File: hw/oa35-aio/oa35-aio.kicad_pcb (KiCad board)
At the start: 6 copper layers, 36 x 36 mm, 283 parts, among them J1 TYPE-C-31-M-12, J10 M1A, J11 M1B, J12 M1C, J13 M2A, J14 M2B, J15 M2C, J16 M3A, J17 M3B, J18 M3C, J19 M4A, J2 SM06B-SRSS-TB, J20 M4B, J21 M4C, J3 BAT+, J4 BAT-, P1 +5V, P10 TX6, P11 RX1, P12 TX1, P13 LED, P14 BZ-, P15 BZ+, P16 RSSI, P17 SCL, P18 SDA, P19 +3V3, P2 GND, P20 GND, P21 VBAT, P22 GND, P3 RX2, P4 TX2, P5 +5V, P6 GND, P7 RX4, P8 TX4, P9 RX6, Q1 2N7002, U1 INA186A3IDCKR, U10 USBLC6-2SC6, U2 LMR51430YFDDCR, U20 AT32F421G8U7, U21 NSG2065Q, U3 LMR51430YFDDCR, U30 AT32F421G8U7, U31 NSG2065Q, U4 LP5912-3.3DRVR, U40 AT32F421G8U7, U41 NSG2065Q, U5 TLV76733DRVR, U50 AT32F421G8U7, U51 NSG2065Q, U6 STM32F722RET6, U7 ICM-42688-P, U8 BMP280, U9 W25Q128JVSIQ, Y1 8MHz

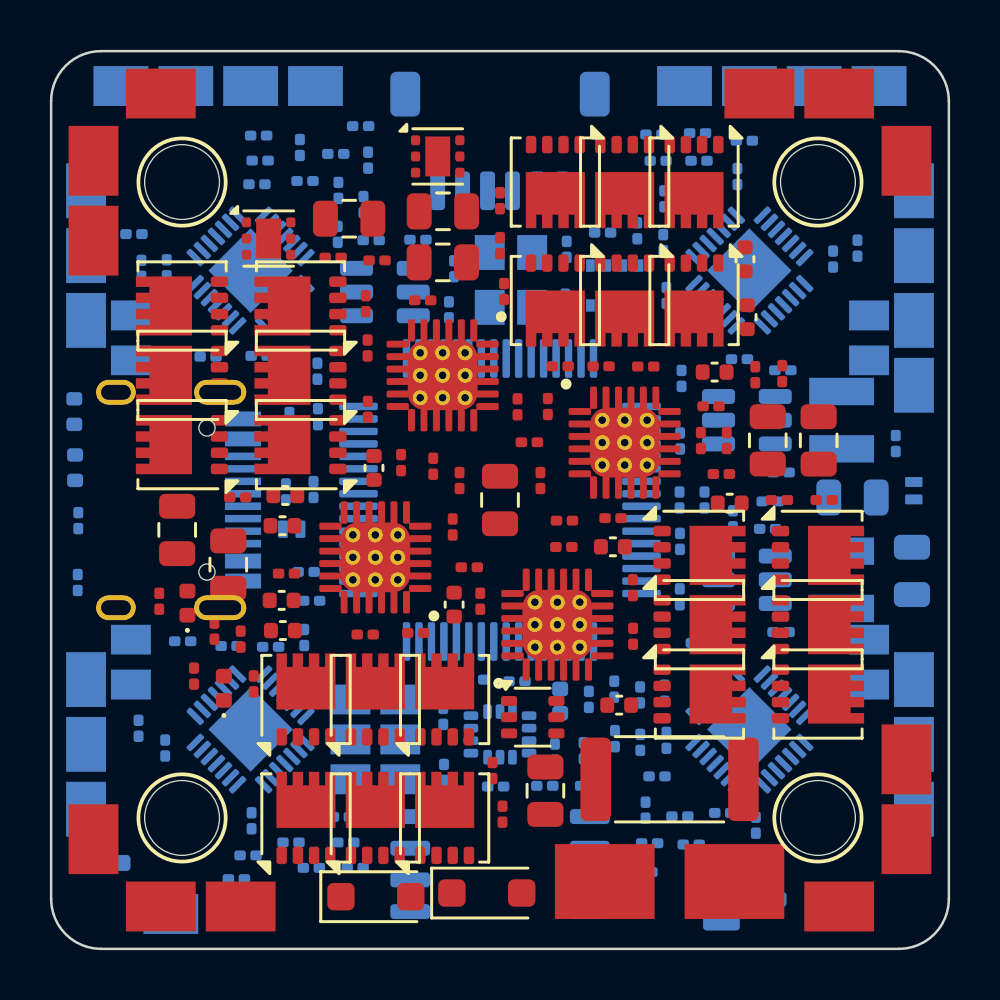
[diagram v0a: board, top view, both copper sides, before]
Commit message: OA35-AIO: fix current-sense input polarity and LDO no-connects
The INA186 in DCK/SC70-6 is 1 REF, 2 GND, 3 VS, 4 IN+, 5 IN-, 6 OUT, per
KiCad's own INA199xxDCK symbol and the OpenESC symbol library. High-side
sensing needs IN+ on the battery side of the shunt; the reference design
wires it the other way round, which would read zero current. Corrected here
and documented.

Also stop tying the LP5912's NC and open-drain power-good pins to rails, and
give the auto-placer "sit next to X" hints so decoupling lands on the pin it
decouples (mean distance 4.6 mm instead of 6.9 mm).

Co-Authored-By: Claude Opus 5 <noreply@anthropic.com>
Claude-Session: https://claude.ai/code/session_013J1rgXZWykCJN7jVVS67P2
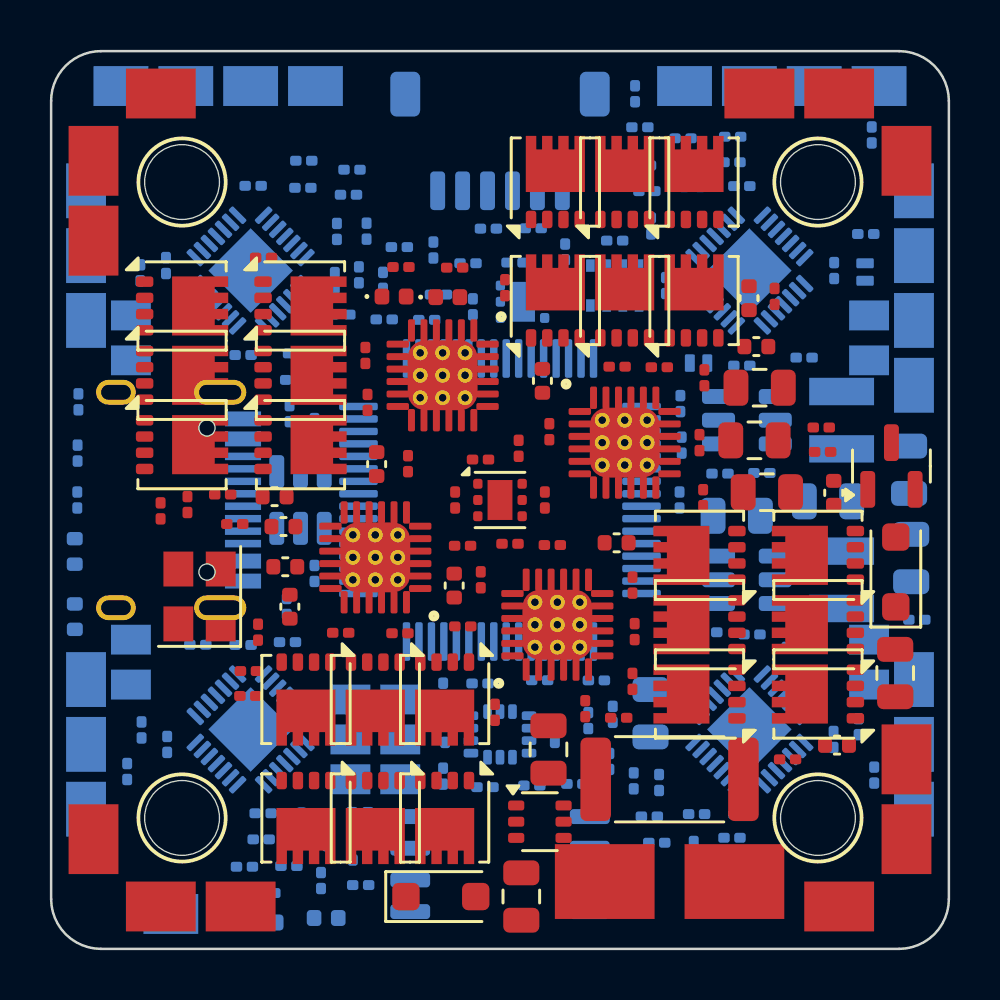
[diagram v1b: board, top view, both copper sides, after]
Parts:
- C10, C11, C16, C17, C18, C24, C25, C26, C29, C30, C38, C40, C41, C9, U5: moved to B.Cu
- C21, C22, C35, C36, Q1, R16, R17, Y1: moved to F.Cu
- moved D4 25.2 mm to (164.6, 90.9), turned to 90 degrees
- moved D2 24.6 mm to (165.9, 102.9), turned to 90 degrees
- moved CVDD2 23.7 mm to (163.4, 90.8), turned to 90 degrees
- moved C4 22.7 mm to (151.9, 110.0), turned to 90 degrees
- moved C41 22.6 mm to (151.3, 111.4)
- moved C40 21.9 mm to (154.6, 89.6), turned to 0 degrees
- moved C2 21.7 mm to (160.2, 97.6), turned to 0 degrees
- moved C6 21.3 mm to (154.8, 108.7), turned to 0 degrees
- moved C33 21.2 mm to (153.9, 107.2), turned to 0 degrees
- moved C9 20.4 mm to (156.0, 108.6)
- moved R12 19.9 mm to (144.1, 86.8), turned to 0 degrees
- moved CVDD3 19.8 mm to (136.7, 109.8), turned to 90 degrees
- moved C38 19.8 mm to (149.4, 111.5), turned to 0 degrees
- moved CVCC4 19.3 mm to (144.6, 94.2), turned to 90 degrees
- moved C37 19.1 mm to (143.9, 87.8)
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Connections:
- U1 pad 4: VBAT -> VBAT_IN
- U1 pad 5: VBAT_IN -> VBAT
- U4 pad 2: +3V3 -> NC_U4_2
- U4 pad 5: GND -> NC_U4_5

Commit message: OA35-AIO: fix motor pad corners, driver thermal vias and placement checks
Three real defects found by reading the DRC report:

- motor pads for channels 3 and 4 were rotated by index rather than by their
  own frame angle, so M3 and M4 landed in each other's corners
- the NSG2065Q land pattern carried thermal vias straight through the board
  into the flight controller's pads underneath; the exposed pad now reaches
  ground through the surrounding pour instead
- the QFN-24 pads were long enough to touch each other at the corners and to
  short to the exposed pad; the geometry now follows the upstream KiCad
  generator (0.775 x 0.25 at 1.9875)

Placement now blocks each through-hole pad on both sides, which caught the
USB-C shell posts sitting on channel 4's MOSFETs; channel 4 moved 4.4 mm
forward to clear them. The mounting hole footprint uses KiCad's own NPTH
form. Board saved before verification so a failing layout can be looked at.

Co-Authored-By: Claude Opus 5 <noreply@anthropic.com>
Claude-Session: https://claude.ai/code/session_013J1rgXZWykCJN7jVVS67P2
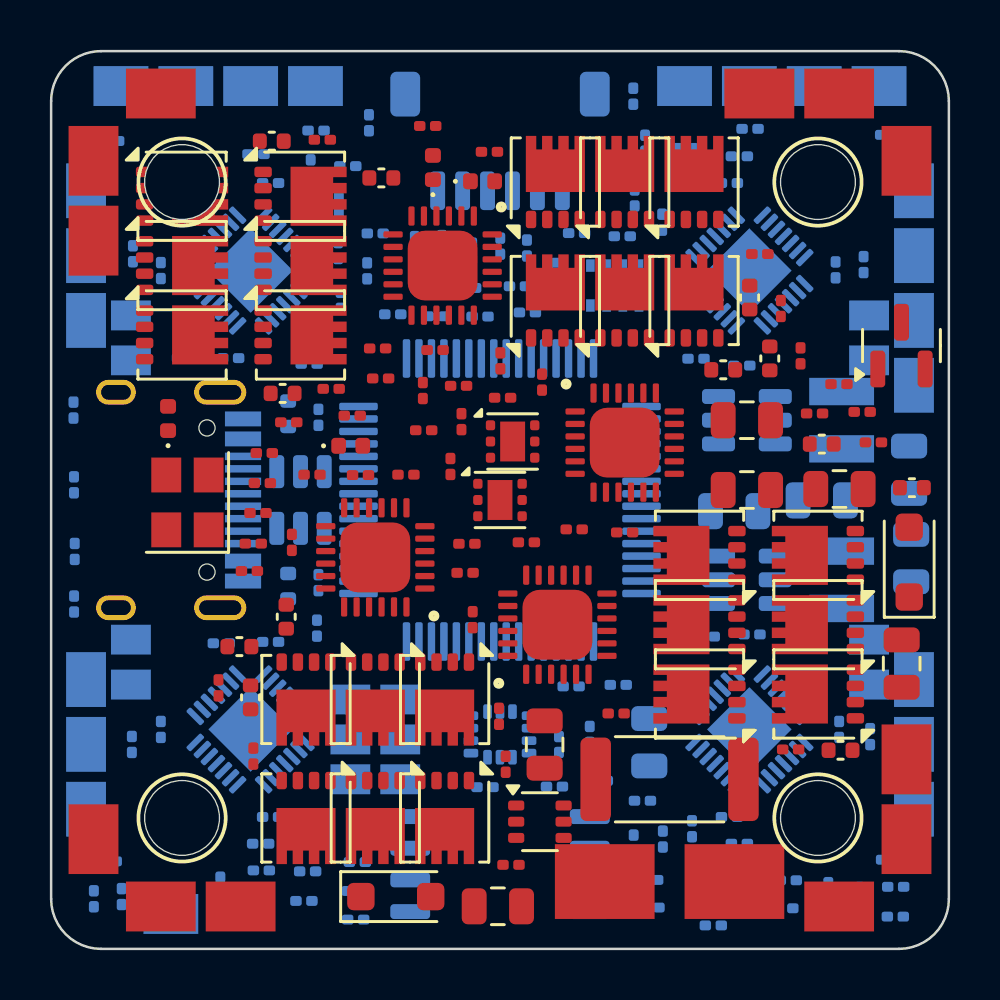
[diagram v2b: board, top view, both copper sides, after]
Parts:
- C23, C24, D7, D8, R10, R11, R13, U5: moved to F.Cu
- moved R12 37.0 mm to (165.9, 116.7)
- moved RNB2 30.5 mm to (134.4, 85.6), turned to 0 degrees
- moved RSIG2 30.3 mm to (165.9, 115.5)
- moved C37 30.0 mm to (133.7, 116.0), turned to 90 degrees
- moved J17 30.0 mm to (136.4, 116.3), turned to 180 degrees
- moved J18 30.0 mm to (133.7, 113.6), turned to 90 degrees
- moved J20 30.0 mm to (133.7, 86.4), turned to -90 degrees
- moved J21 30.0 mm to (136.4, 83.7), turned to 180 degrees
- moved R13 29.4 mm to (150.4, 114.6)
- moved RSIG4 28.8 mm to (134.8, 115.9)
- moved RNC4 28.3 mm to (144.2, 115.7)
- moved RNA2 27.7 mm to (137.4, 94.3)
- moved J16 27.3 mm to (139.6, 116.3), turned to 180 degrees
- moved J19 27.3 mm to (133.7, 89.6), turned to -90 degrees
- moved R15 23.6 mm to (134.3, 114.5), turned to 0 degrees
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
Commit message: OA35-AIO: keep capacitor footprints honest against their LCSC parts
The 4.7 uF, 1 uF and 20 pF capacitors were being emitted on the 0201 land
pattern while their LCSC parts are 0402, so the BOM and the board disagreed
about the physical part. C() now picks the footprint from the value the same
way R() does, and the BOM prints readable values.

Co-Authored-By: Claude Opus 5 <noreply@anthropic.com>
Claude-Session: https://claude.ai/code/session_013J1rgXZWykCJN7jVVS67P2
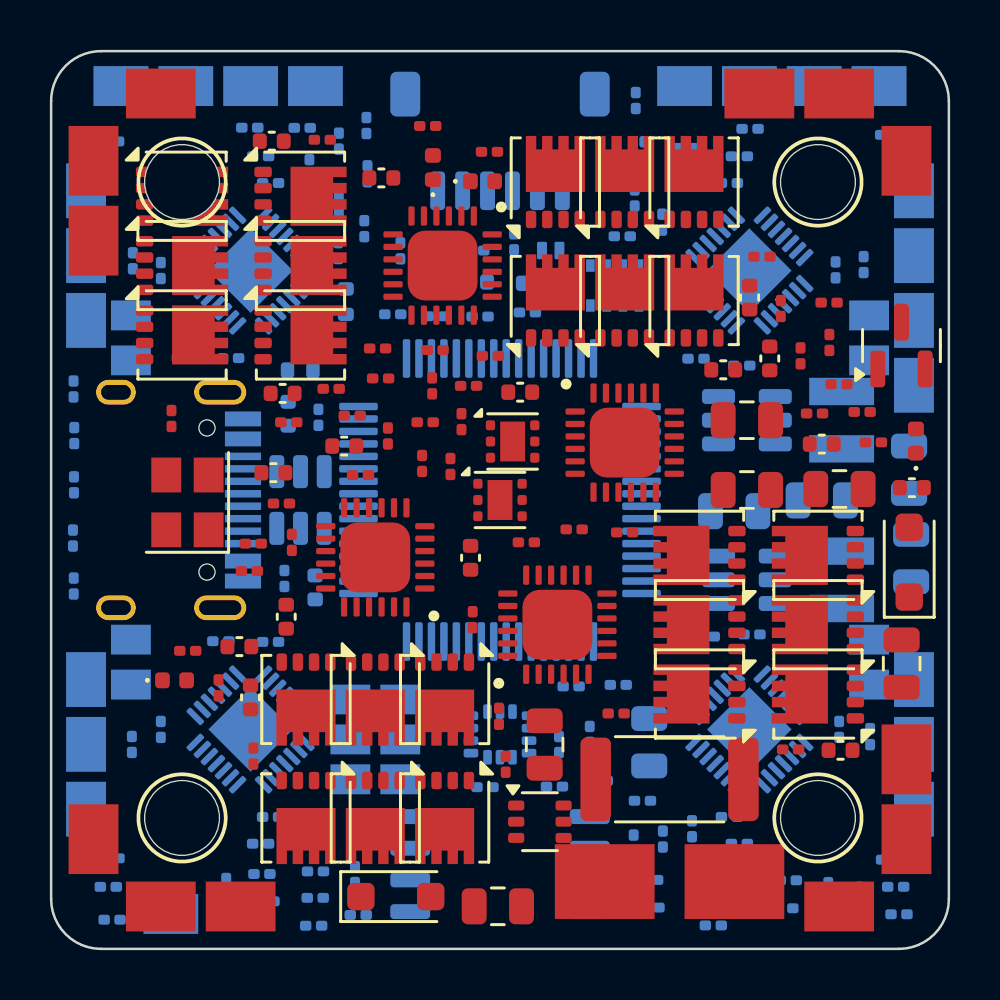
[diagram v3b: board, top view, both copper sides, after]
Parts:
- C19, C23, C30, C31, C33, C35, C36, C43: footprint Capacitor_SMD:C_0201_0603Metric -> Capacitor_SMD:C_0402_1005Metric
- C37, R12: moved to F.Cu
- R11: moved to B.Cu
- moved R11 31.5 mm to (166.0, 116.6)
- moved D8 30.0 mm to (166.7, 97.6)
- moved R12 27.4 mm to (147.0, 96.9)
- moved R13 22.5 mm to (136.8, 96.7), turned to 90 degrees
- moved C37 22.0 mm to (145.5, 97.4)
- moved R16 16.6 mm to (163.2, 93.7), turned to 90 degrees
- moved RNB2 16.0 mm to (132.9, 101.5), turned to 90 degrees
- moved D7 11.8 mm to (136.9, 107.2)
- moved RCC4 10.4 mm to (134.4, 85.6), turned to 0 degrees
- moved RRST2 10.2 mm to (155.4, 84.0), turned to 90 degrees
- moved C43 10.2 mm to (141.5, 96.5)
- moved RGBH2 10.2 mm to (160.5, 90.2), turned to 0 degrees
- moved RNC4 9.88 mm to (134.4, 114.4)
- moved RBT02 9.77 mm to (165.6, 85.4), turned to 0 degrees
- moved RBC4 9.41 mm to (135.3, 90.4)
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
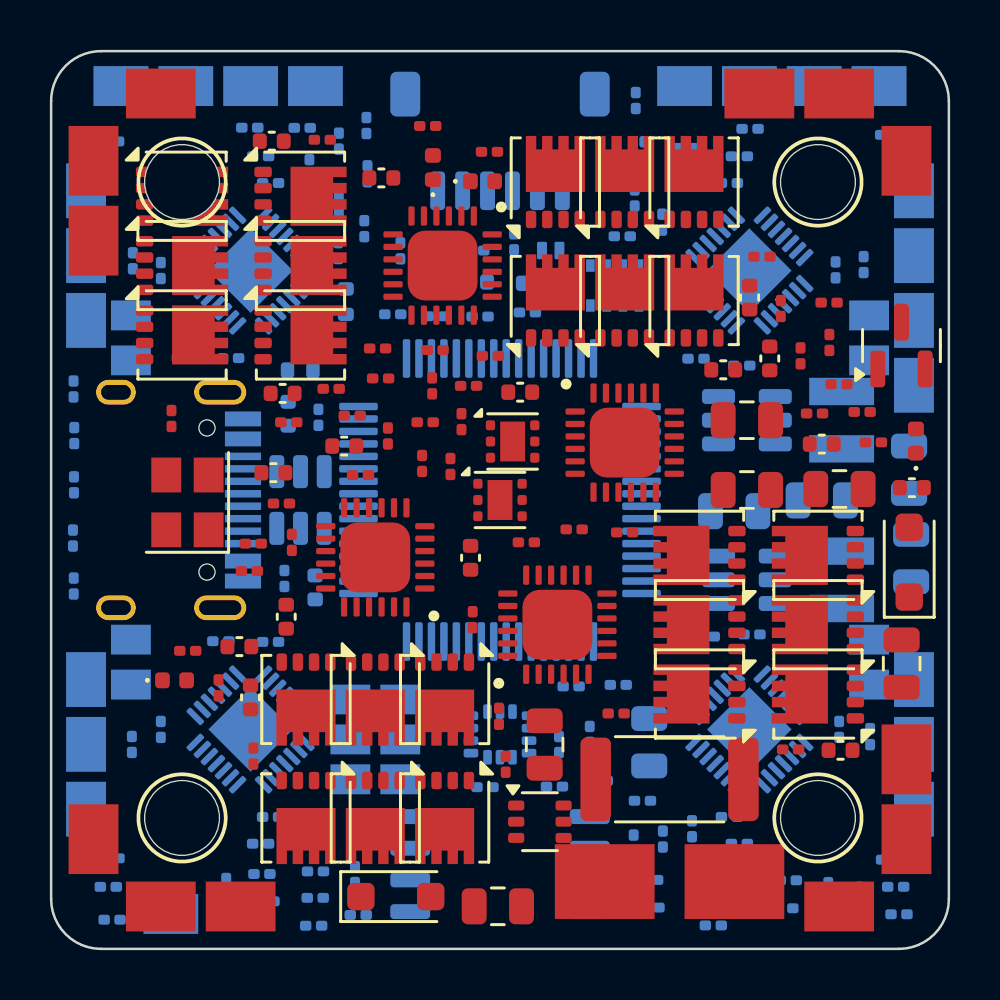
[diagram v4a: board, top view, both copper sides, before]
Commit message: OA35-AIO: stitch plane nets with vias, and stop handing planes to the router
Two findings from reading what actually came back from freerouting:

- It treats GND and VBAT as planes needing no routing, which is only true of
  through-hole pads, so every surface-mount pad on those nets came back with
  nothing tying it to the inner copper. tools/stitch.py now drops a via
  beside (or on) each of them plus a sparse grid tying the outer pours to
  the planes, checked against pad, track and via geometry rather than
  bounding boxes.
- Exporting the planes to the router made it worse, not better: with them it
  routed 75 nets out of 279 in seventeen minutes and left the rest bare.
  The pours are now added only after routing.

finish_pcb.py strips its own previous output first, in a subprocess, because
pcbnew's python proxies stop working after BOARD.Remove() for the rest of the
interpreter.

Co-Authored-By: Claude Opus 5 <noreply@anthropic.com>
Claude-Session: https://claude.ai/code/session_013J1rgXZWykCJN7jVVS67P2
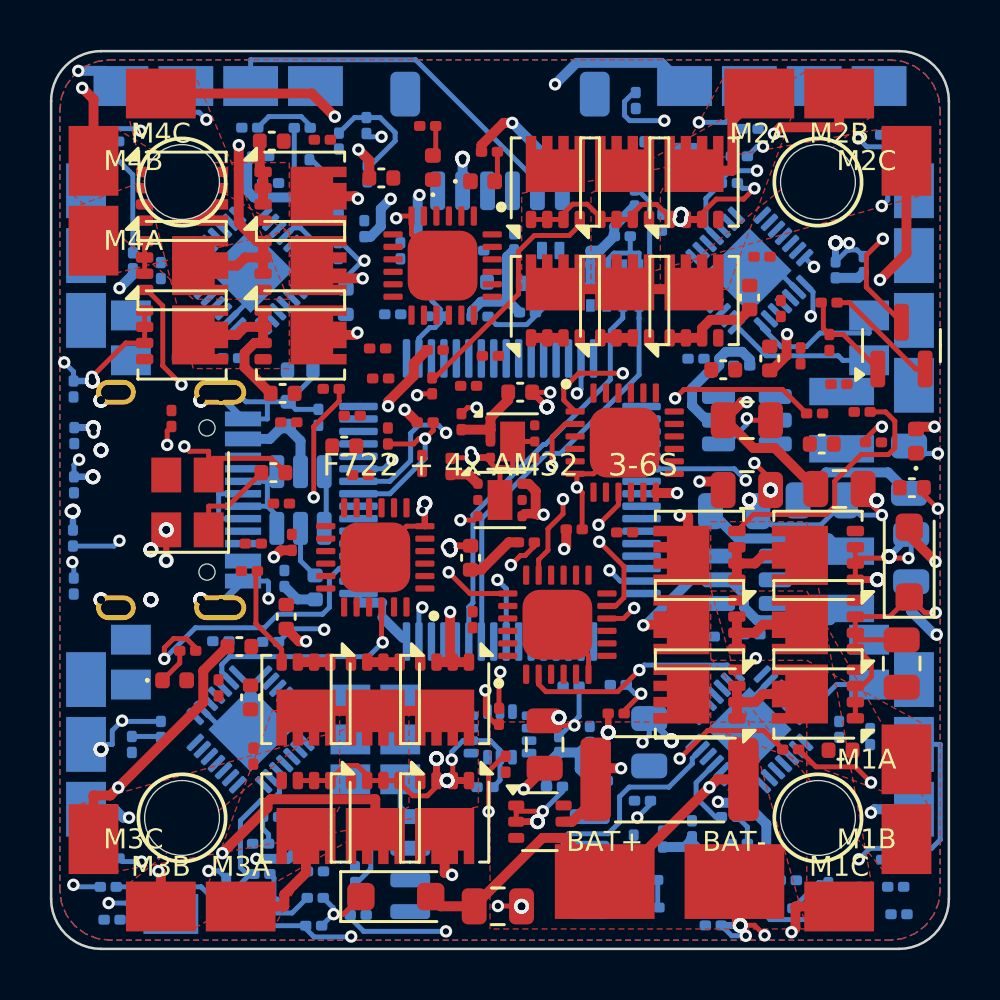
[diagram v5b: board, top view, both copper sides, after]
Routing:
- net GND: track 0.00 -> 231.8 mm, vias 0 -> 129
- net +5V: track 0.00 -> 84.6 mm, vias 0 -> 6
- net +3V3: track 0.00 -> 46.5 mm, vias 0 -> 2
- net PH_C_3: track 0.00 -> 45.4 mm, vias 0 -> 4
- net VBAT: track 0.00 -> 45.0 mm, vias 0 -> 16
- net PAD_BZ-: track 0.00 -> 42.9 mm, vias 0 -> 2
- net CURR: track 0.00 -> 37.7 mm, vias 0 -> 3
- net PAD_RSSI: track 0.00 -> 37.3 mm, vias 0 -> 2
- net ADC_RSSI: track 0.00 -> 31.8 mm, vias 0 -> 2
- net VBAT_IN: track 0.00 -> 30.9 mm, vias 0 -> 2
- net PH_B_4: track 0.00 -> 30.1 mm, vias 0 -> 4
- net PH_C_4: track 0.00 -> 27.0 mm, vias 0 -> 2
- net PH_B_3: track 0.00 -> 26.1 mm, vias 0 -> 3
- net PH_B_2: track 0.00 -> 23.7 mm, vias 0 -> 2
- net FBB_2: track 0.00 -> 23.2 mm, vias 0 -> 2
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- added copper zone on B.Cu, net GND
- added copper zone on F.Cu, net GND
- added copper zone on In4.Cu, net GND
- added copper zone on F.Cu, net PH_A_1
- added copper zone on F.Cu, net PH_A_2
- added copper zone on F.Cu, net PH_A_3
- added copper zone on F.Cu, net PH_A_4
- added copper zone on F.Cu, net PH_B_1
- added copper zone on F.Cu, net PH_B_2
- added copper zone on F.Cu, net PH_B_3
- added copper zone on F.Cu, net PH_B_4
- added copper zone on F.Cu, net PH_C_1
- added copper zone on F.Cu, net PH_C_2
- added copper zone on F.Cu, net PH_C_3
- added copper zone on F.Cu, net PH_C_4
- added copper zone on F.Cu, net VBAT_IN
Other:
- board text added: "+3V3"
- board text added: "+5V"
- board text added: "BAT+"
- board text added: "BAT-"
- board text added: "BOOT0"
- board text added: "BZ+"
- board text added: "BZ-"
- board text added: "F722 + 4x AM32 3-6S"
- board text added: "GND"
- board text added: "LED"
- board text added: "M1A"
- board text added: "M1B"
- board text added: "M1C"
- board text added: "M2A"
- board text added: "M2B"
- board text added: "M2C"
- board text added: "M3A"
- board text added: "M3B"
- board text added: "M3C"
- board text added: "M4A"
- board text added: "M4B"
- board text added: "M4C"
- board text added: "NRST"
- board text added: "OA35-AIO rev A"
- board text added: "RSSI"
- board text added: "RX1"
- board text added: "RX2"
- board text added: "RX4"
- board text added: "RX6"
- board text added: "SCL"
- board text added: "SDA"
- board text added: "SWCLK"
- board text added: "SWCLK1"
- board text added: "SWCLK2"
- board text added: "SWCLK3"
- board text added: "SWCLK4"
- board text added: "SWDIO"
- board text added: "SWDIO1"
- board text added: "SWDIO2"
- board text added: "SWDIO3"
- board text added: "SWDIO4"
- board text added: "TX1"
- board text added: "TX2"
- board text added: "TX4"
- board text added: "TX6"
- board text added: "VBAT"
